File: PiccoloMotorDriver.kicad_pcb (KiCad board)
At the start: 2 copper layers, 83 parts, among them J6 Connector, USB-TYPE-C-16P, U1 SP485EEN, U2 XC6210B332MR, U3 XL1509, U4 TJA1050T/CM,118, U5 AS5047D, U6 USBLC6-2SC6, U7 STM32H723VGHx, U8 DRV8316RRGFR, X2 X322516MLB4SI

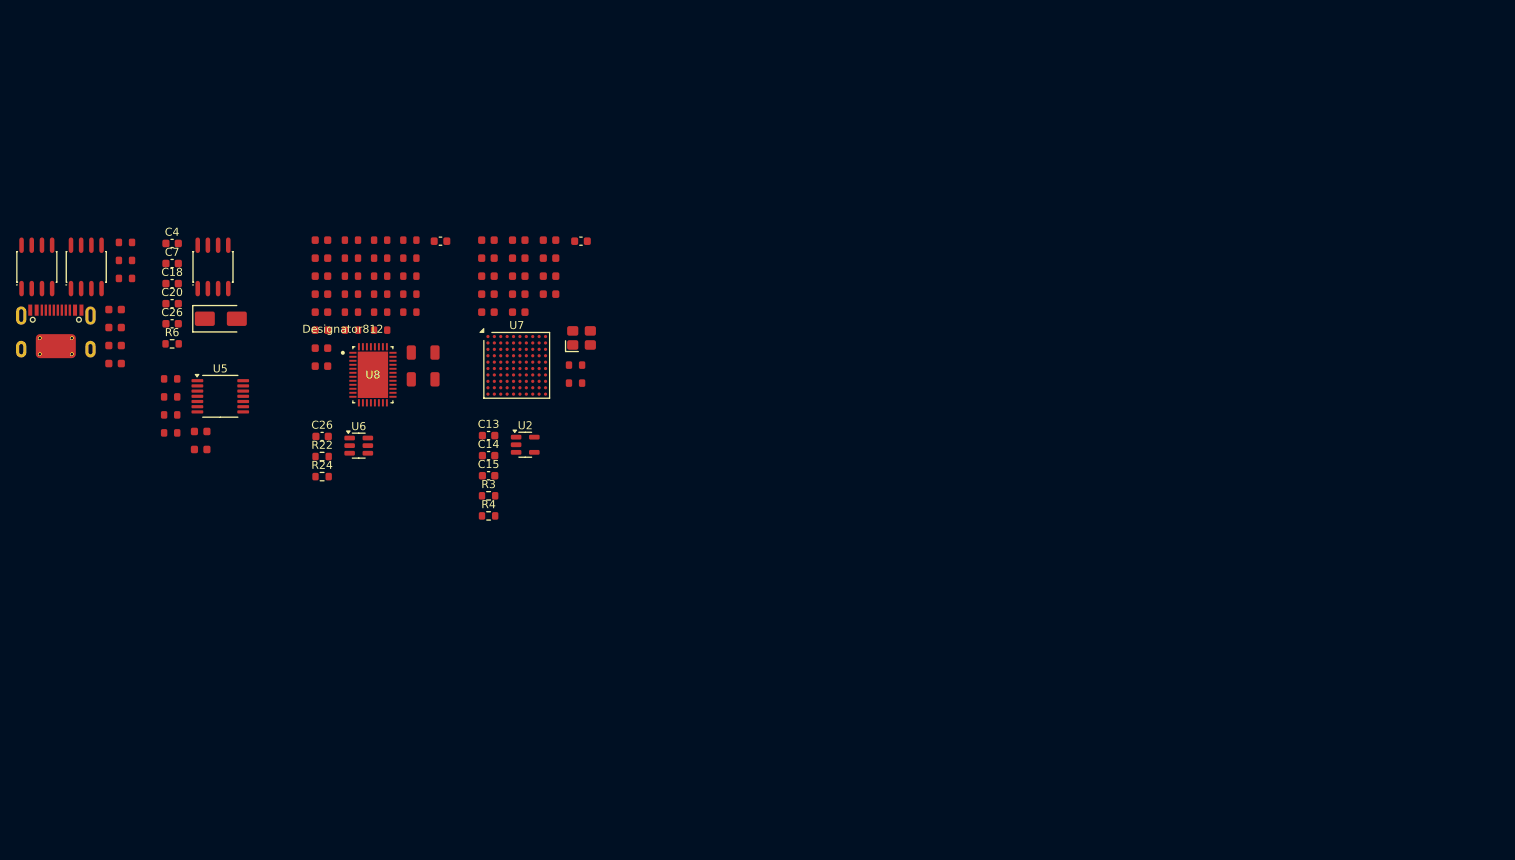
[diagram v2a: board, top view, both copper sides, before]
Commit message: Added DRV layout
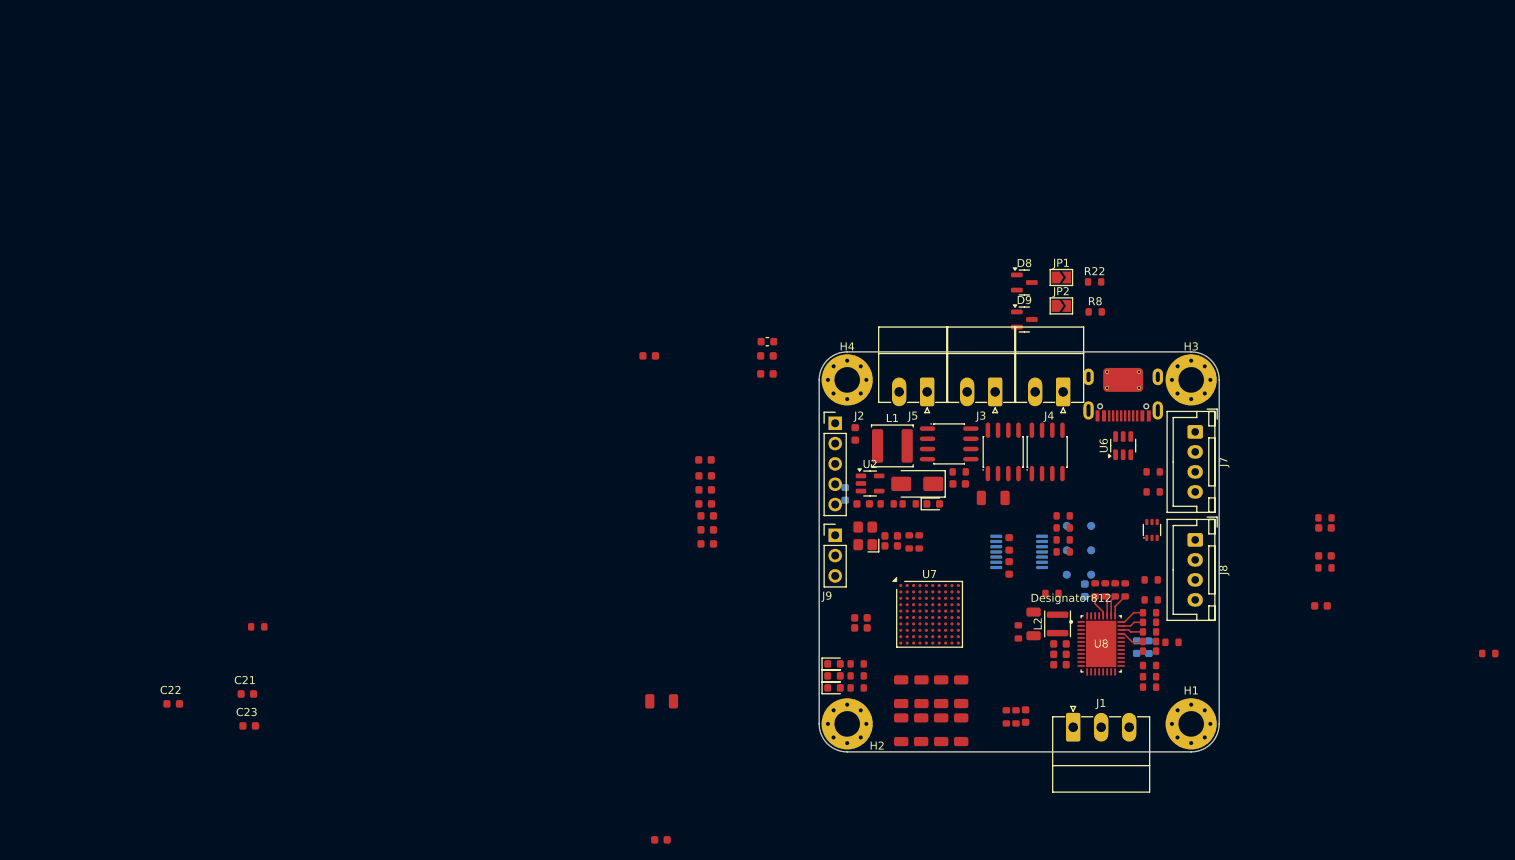
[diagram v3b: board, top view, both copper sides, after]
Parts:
- removed C20, C26: 10uF/0603, Capacitor_SMD:C_0603_1608Metric
- removed C26: 100nF/0603, Capacitor_SMD:C_0603_1608Metric
- removed the R22 at (80.3, 85.8)
- removed the R22 at (104.9, 108.1)
- removed the R24 at (104.9, 110.6)
- added C39: 100nF, PCM_JLCPCB:C_0603, F.Cu at (192.8, 140.5)
- added C40: 10uF, PCM_JLCPCB:C_1206, F.Cu at (182.2, 142.2)
- added C41: 10uF, PCM_JLCPCB:C_1206, F.Cu at (179.8, 137.5)
- added C42: 10uF, PCM_JLCPCB:C_1206, F.Cu at (182.2, 137.5)
- added C43: 10uF, PCM_JLCPCB:C_1206, F.Cu at (184.8, 137.5)
- added C44: 10uF, PCM_JLCPCB:C_1206, F.Cu at (177.2, 142.2)
- added C45: 10uF, PCM_JLCPCB:C_1206, F.Cu at (179.8, 142.2)
- added C46: 100nF, PCM_JLCPCB:C_0603, F.Cu at (171.5, 105.2)
- added D1: H5VUT3UA, PCM_JLCPCB:SOT-363_L2.1-W1.3-P0.65-LS2.2-BL, F.Cu at (208.6, 117.3)
- added D4: Red, PCM_JLCPCB:D_0603, F.Cu at (168.8, 134.0)
- added D5: Yellow, PCM_JLCPCB:D_0603, F.Cu at (181.2, 114.0)
- added D6: White, PCM_JLCPCB:D_0603, F.Cu at (168.8, 135.5)
- added D7: Yellow, PCM_JLCPCB:D_0603, F.Cu at (168.8, 137.0)
- added D8: NUP2105L, Package_TO_SOT_SMD:SOT-23, F.Cu at (192.6, 86.3)
- added D9: NUP2105L, Package_TO_SOT_SMD:SOT-23, F.Cu at (192.6, 91.0)
- added H1: MountingHole_Pad, MountingHole:MountingHole_3.2mm_M3_Pad_Via, F.Cu at (213.5, 141.5)
- added H2: MountingHole_Pad, MountingHole:MountingHole_3.2mm_M3_Pad_Via, F.Cu at (170.5, 141.5)
- added H3: MountingHole_Pad, MountingHole:MountingHole_3.2mm_M3_Pad_Via, F.Cu at (213.5, 98.5)
- added H4: MountingHole_Pad, MountingHole:MountingHole_3.2mm_M3_Pad_Via, F.Cu at (170.5, 98.5)
- added J1: 01x03_MotorTerminal, Connector_Phoenix_MC:PhoenixContact_MC_1,5_3-G-3.5_1x03_P3.50mm_Horizontal, F.Cu at (198.8, 141.9)
- added J2: Conn_01x05_SWD, Connector_PinHeader_2.54mm:PinHeader_1x05_P2.54mm_Vertical, F.Cu at (169.0, 103.9)
- added J3: Screw_Terminal_01x02_CAN, Connector_Phoenix_MC:PhoenixContact_MC_1,5_2-G-3.5_1x02_P3.50mm_Horizontal, F.Cu at (189.0, 100.0)
- added J4: Screw_Terminal_01x02_RS485, Connector_Phoenix_MC:PhoenixContact_MC_1,5_2-G-3.5_1x02_P3.50mm_Horizontal, F.Cu at (197.5, 100.0)
- added J5: Screw_Terminal_01x02_POWER, Connector_Phoenix_MC:PhoenixContact_MC_1,5_2-G-3.5_1x02_P3.50mm_Horizontal, F.Cu at (180.5, 100.0)
- added J7: EXT_AN, Connector_JST:JST_XH_B4B-XH-A_1x04_P2.50mm_Vertical, F.Cu at (214.0, 105.0)
- added J8: Q_ENCODER, Connector_JST:JST_XH_B4B-XH-A_1x04_P2.50mm_Vertical, F.Cu at (214.0, 118.5)
- added J9: Conn_01x03, Connector_PinHeader_2.54mm:PinHeader_1x03_P2.54mm_Vertical, F.Cu at (169.0, 117.9)
- added JP1: 120R Load, Jumper:SolderJumper-2_P1.3mm_Open_TrianglePad1.0x1.5mm, F.Cu at (197.3, 85.7)
- added JP2: 120R Load, Jumper:SolderJumper-2_P1.3mm_Open_TrianglePad1.0x1.5mm, F.Cu at (197.3, 89.2)
- added L1: 68uH, 1A (JLC-C96920), Inductor_SMD:L_Changjiang_FNR5020S, F.Cu at (176.2, 106.8)
- added L2: 47uH, 200mA (JLC-C83420), Inductor_SMD:L_Changjiang_FNR3010S, F.Cu at (196.8, 129.0)
- added R22: 120Ω, PCM_JLCPCB:R_0603, F.Cu at (201.4, 86.2)
- added R30: 100Ω, PCM_JLCPCB:R_0603, F.Cu at (208.5, 123.5)
- added R31: 1kΩ, PCM_JLCPCB:R_0603, F.Cu at (191.6, 140.6)
- added R32: 47kΩ, PCM_JLCPCB:R_0603, F.Cu at (190.4, 140.6)
- added R33: 100Ω, PCM_JLCPCB:R_0603, F.Cu at (208.8, 112.5)
- added R34: 0Ω, PCM_JLCPCB:R_0603, F.Cu at (191.9, 130.0)
- added R35: 100Ω, PCM_JLCPCB:R_0603, F.Cu at (208.5, 126.0)
- added R36: 100Ω, PCM_JLCPCB:R_0603, F.Cu at (208.8, 110.0)
- added R37: 680Ω, PCM_JLCPCB:R_0603, F.Cu at (171.8, 135.5)
- added R38: 1kΩ, PCM_JLCPCB:R_0603, F.Cu at (171.8, 134.0)
- added R39: 680Ω, PCM_JLCPCB:R_0603, F.Cu at (171.8, 137.0)
- added TP1: A, TestPoint:TestPoint_Pad_D1.0mm, B.Cu at (197.9, 116.8)
- added TP2: B, TestPoint:TestPoint_Pad_D1.0mm, B.Cu at (201.0, 116.8)
- added TP3: I, TestPoint:TestPoint_Pad_D1.0mm, B.Cu at (197.9, 119.8)
- added TP4: U, TestPoint:TestPoint_Pad_D1.0mm, B.Cu at (201.0, 119.8)
- added TP5: V, TestPoint:TestPoint_Pad_D1.0mm, B.Cu at (197.9, 122.8)
- added TP6: W/PWM, TestPoint:TestPoint_Pad_D1.0mm, B.Cu at (201.0, 122.8)
- C11, C12, C19, FB1, U5: moved to B.Cu
- C13, C18, C4: value 100nF/0603 -> 100nF; footprint Capacitor_SMD:C_0603_1608Metric -> PCM_JLCPCB:C_0603
- C14: value 100nF/0603 -> 10uF; footprint Capacitor_SMD:C_0603_1608Metric -> PCM_JLCPCB:C_1206
- C15, C7: value 10uF/0603 -> 10uF; footprint Capacitor_SMD:C_0603_1608Metric -> PCM_JLCPCB:C_1206
- R3, R6: value 1K -> 1kΩ; footprint Resistor_SMD:R_0603_1608Metric -> PCM_JLCPCB:R_0603
- R4: value 0 -> 1kΩ; footprint Resistor_SMD:R_0603_1608Metric -> PCM_JLCPCB:R_0603
- moved R1 151.3 mm to (250.7, 132.7)
- moved J6 133.7 mm to (205.0, 100.5), turned to 180 degrees
- moved C27 133.0 mm to (229.7, 126.8)
- moved C6 130.2 mm to (230.2, 120.5)
- moved C5 129.9 mm to (230.2, 117.0)
- moved U1 128.4 mm to (195.5, 107.5)
- moved R7 125.8 mm to (230.2, 122.0)
- moved R5 125.4 mm to (230.2, 115.8)
- moved R8 121.5 mm to (201.5, 90.0)
- moved U4 116.9 mm to (190.0, 107.5)
- moved R24 113.6 mm to (197.5, 120.0), turned to 180 degrees
- moved R27 113.0 mm to (197.5, 118.5), turned to 180 degrees
- moved R28 112.5 mm to (197.5, 117.0), turned to 180 degrees
- moved R29 112.0 mm to (197.5, 115.5), turned to 180 degrees
- moved R2 112.0 mm to (208.3, 134.2), turned to 180 degrees
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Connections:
- net DRV_SO_A renamed AN_DRV_SO_A
- C10 pad 1: +5V -> Net-(U8-FB_BK)
- C11 pad 1: DRV_AN_REF -> AN_DRV_AN_REF
- C13 pad 1: GND -> +3.3V
- C13 pad 2: +5V -> GND
- C14 pad 1: GND -> +3.3V
- C14 pad 2: +3.3V -> GND
- C15 pad 1: GND -> +5V
- C15 pad 2: +3.3V -> GND
- C17 pad 2: GNDPWR -> GND
- C18 pad 1: GND -> +5V
- C18 pad 2: +5V -> GND
- C38 pad 2: GNDPWR -> GND
- C4 pad 1: GND -> Vdrive
- C4 pad 2: Vdrive -> GND
- C5 pad 1: DRV_SO_B -> AN_DRV_SO_B
- C6 pad 1: DRV_SO_C -> AN_DRV_SO_C
- C7 pad 1: GND -> Vdrive
- C7 pad 2: Vdrive -> GND
- R1 pad 1: ~{FAULT} -> ~{DRV_FAULT}
- R14 pad 1: ~{FAULT} -> ~{DRV_FAULT}
- R15 pad 1: ~{SLEEP} -> ~{DRV_SLEEP}
- R3 pad 1: +5V -> Net-(D5-Pad1)
- R3 pad 2: Net-(U2-CE) -> GND
- R4 pad 1: GND -> Net-(U2-CE)
- R4 pad 2: GNDPWR -> +5V
- R5 pad 1: DRV_SO_B -> AN_DRV_SO_B
- R6 pad 1: GND -> Net-(U3-ON/OFF)
- R6 pad 2: Net-(U3-ON/OFF) -> GND
- R7 pad 1: DRV_SO_C -> AN_DRV_SO_C
- U7 pad A8: RS485_DE -> unconnected-(U7-PA15(JTDI)-PadA8)
- U7 pad B7: unconnected-(U7-PD2-PadB7) -> DEBUG_TX
- U7 pad E10: unconnected-(U7-PC7-PadE10) -> QUAD_ENC_B
- U7 pad F1: unconnected-(U7-PC0-PadF1) -> AN_EXT_IN_1
- U7 pad F10: unconnected-(U7-PC6-PadF10) -> QUAD_ENC_A
- U7 pad F3: unconnected-(U7-PC3_C-PadF3) -> AN_DRV_SO_C
- U7 pad F9: unconnected-(U7-PC8-PadF9) -> DRV_OFF
- U7 pad G4: DRV_AN_REF -> AN_DRV_SO_B
- U7 pad G5: unconnected-(U7-PB2-PadG5) -> ~{DRV_SLEEP}
- U7 pad H4: unconnected-(U7-PC5-PadH4) -> AN_VBUS
- U7 pad J4: unconnected-(U7-PB0-PadJ4) -> AN_EXT_IN_0
- U7 pad K3: DRV_SO_B -> DRV_AN_REF
- U7 pad K4: DRV_SO_C -> ~{DRV_FAULT}
- U8 pad 12: GNDPWR -> GND
- U8 pad 15: GNDPWR -> GND
- U8 pad 18: GNDPWR -> GND
- U8 pad 3: +5V -> Net-(U8-FB_BK)
- U8 pad 37: DRV_AN_REF -> AN_DRV_AN_REF
- U8 pad 41: GNDPWR -> GND
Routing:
- net Net-(U8-INLC): track 0.00 -> 3.21 mm
- net Net-(U8-INHB): track 0.00 -> 3.20 mm
- net Net-(U8-SDO): track 0.00 -> 2.95 mm
- net Net-(U8-INHC): track 0.00 -> 2.92 mm
- net Net-(U8-SCS_N): track 0.00 -> 2.84 mm
- net Net-(U8-INLB): track 0.00 -> 2.83 mm
- net Net-(U8-SDI): track 0.00 -> 2.64 mm
- net Net-(U8-SCLK): track 0.00 -> 2.53 mm
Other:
- board outline added: 50 x 50 mm
- copper layers 2 -> 4

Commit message: Re arrange connectors
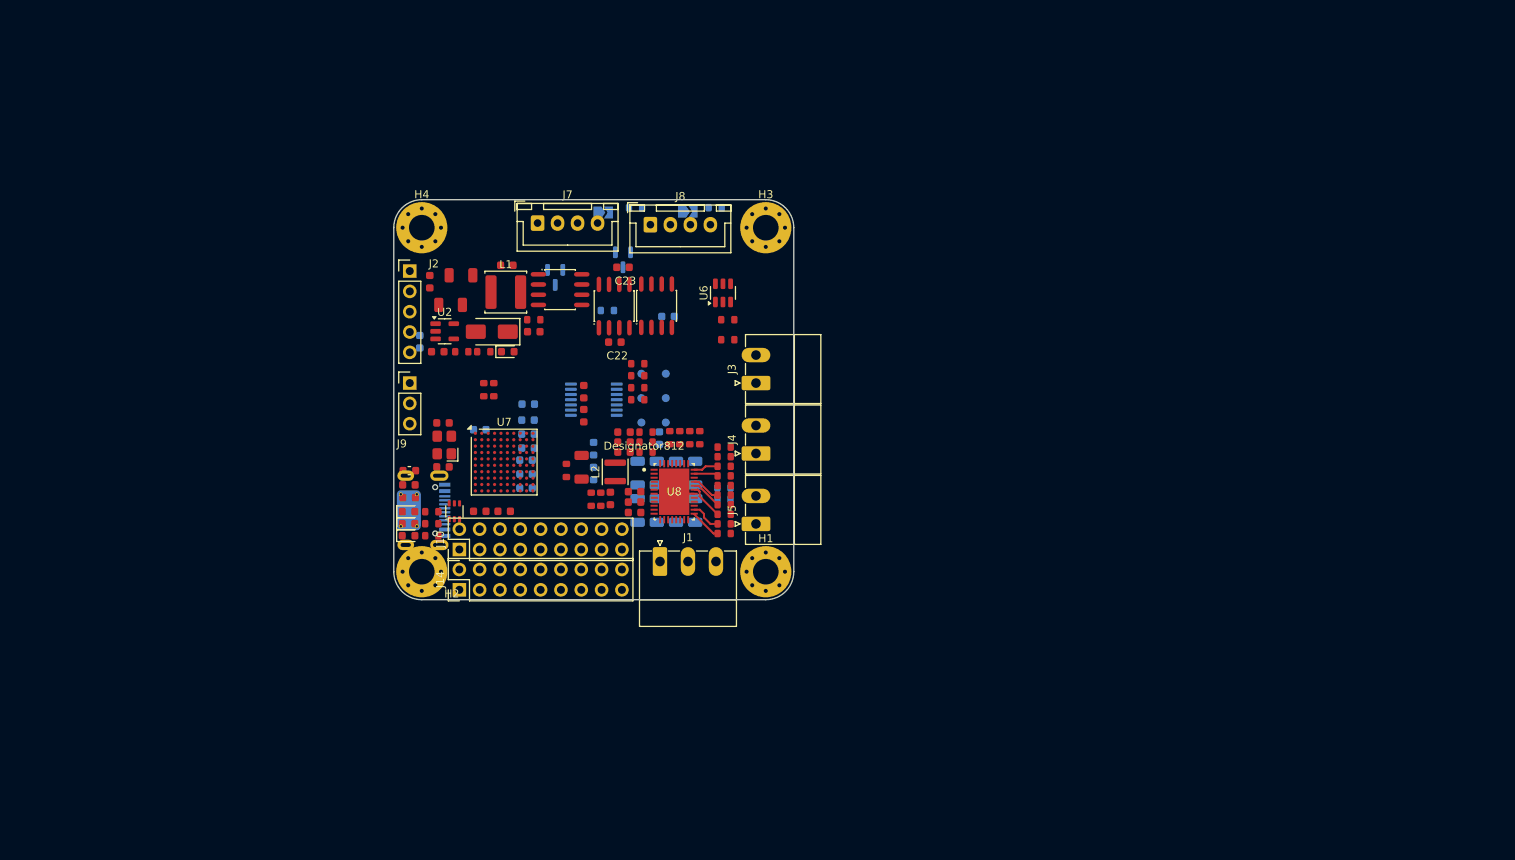
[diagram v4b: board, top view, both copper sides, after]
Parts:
- added J10: Conn_02x09_Odd_Even, Connector_PinHeader_2.54mm:PinHeader_2x09_P2.54mm_Vertical, F.Cu at (122.0, 119.7)
- added J14: Conn_02x09_Odd_Even, Connector_PinHeader_2.54mm:PinHeader_2x09_P2.54mm_Vertical, F.Cu at (122.0, 124.7)
- C21, C3, C30, C31, C32, C33, C34, C35, C36, C38, C40, C41, C42, C43, C44, C45, C7, D8, D9, J6, JP1, JP2, R1, R15, R21, R22, R8: moved to B.Cu
- moved R1 97.8 mm to (155.1, 112.0)
- moved C27 89.2 mm to (142.6, 107.5), turned to 180 degrees
- moved C6 89.0 mm to (142.6, 105.0), turned to 180 degrees
- moved J6 88.5 mm to (117.7, 114.8), turned to 90 degrees
- moved C5 88.3 mm to (142.6, 106.3), turned to 180 degrees
- moved D1 87.2 mm to (121.4, 114.9)
- moved R7 86.6 mm to (145.4, 105.0)
- moved J7 86.2 mm to (131.8, 78.9), turned to 0 degrees
- moved R5 85.4 mm to (145.4, 106.3)
- moved J8 78.7 mm to (145.9, 79.1), turned to 0 degrees
- moved C4 74.4 mm to (128.0, 84.2)
- moved C23 74.0 mm to (142.5, 84.4), turned to 180 degrees
- moved FB1 73.7 mm to (138.8, 107.1)
- moved C15 72.1 mm to (122.2, 85.4)
- moved C22 71.4 mm to (141.5, 93.8), turned to 180 degrees
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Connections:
- R37 pad 1: unconnected-(R37-Pad1) -> UI_LED_YELLOW
- R38 pad 1: unconnected-(R38-Pad1) -> UI_LED_RED
- R39 pad 1: unconnected-(R39-Pad1) -> UI_LED_BLUE
- U7 pad A3: unconnected-(U7-PE2-PadA3) -> /Mcu/PE2
- U7 pad C4: unconnected-(U7-PE1-PadC4) -> /Mcu/PE1
- U7 pad D4: unconnected-(U7-PE0-PadD4) -> /Mcu/PE0
- U7 pad G2: unconnected-(U7-PA0-PadG2) -> UI_LED_RED
- U7 pad H2: unconnected-(U7-PA1-PadH2) -> UI_LED_YELLOW
- U7 pad J2: unconnected-(U7-PA2-PadJ2) -> UI_LED_BLUE
- U7 pad K2: unconnected-(U7-PA3-PadK2) -> RS485_DE
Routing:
- net Net-(U8-INHA): track 0.00 -> 4.55 mm
- net Net-(U8-DRVOFF): track 0.00 -> 3.98 mm
- net Net-(U8-FAULT_N): track 0.00 -> 3.93 mm
- net Net-(U8-INLA): track 0.00 -> 3.91 mm
- net Net-(U8-SDO): track 2.95 -> 0.00 mm
- net Net-(U8-SCS_N): track 2.84 -> 0.00 mm
- net Net-(U8-INLB): track 2.83 -> 0.00 mm
- net Net-(U8-SDI): track 2.64 -> 0.00 mm
- net GND: track 0.00 -> 2.61 mm
- net Net-(U8-SCLK): track 2.53 -> 0.00 mm
- added copper zone on In1.Cu, net GND
